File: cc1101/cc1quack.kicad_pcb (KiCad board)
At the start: 4 copper layers, 59 x 39 mm, 72 parts, among them J103 Conn_01x06_Pin, J201 USB_C_Receptacle, J401 Conn_ARM_JTAG_SWD_10, J402 Conn_01x02, J501 Conn_Coaxial, SW401 Alps SKRTLAE010, U301 XC6206P332MR, U401 STM32F401RCT6, U501 Ebyte-E07-900MM10S, Y401 8MHz 20pF

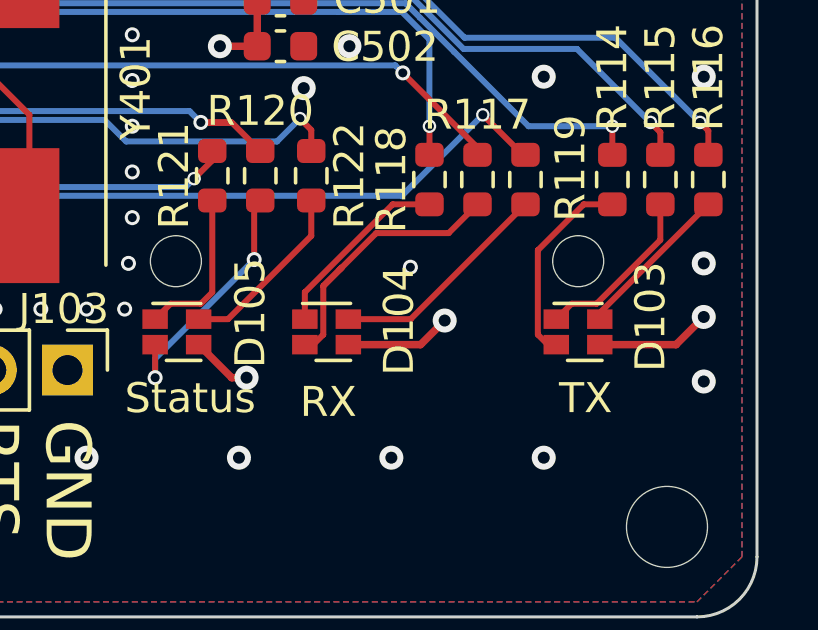
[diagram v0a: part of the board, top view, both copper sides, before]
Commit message: cc1quack: Specialize LiteOn LTST C19HE1WT footprint
Specialize LiteOn LTST C19HE1WT footprint to include 3D models.

Signed-off-by: Andreas Sandberg <andreas@sandberg.uk>
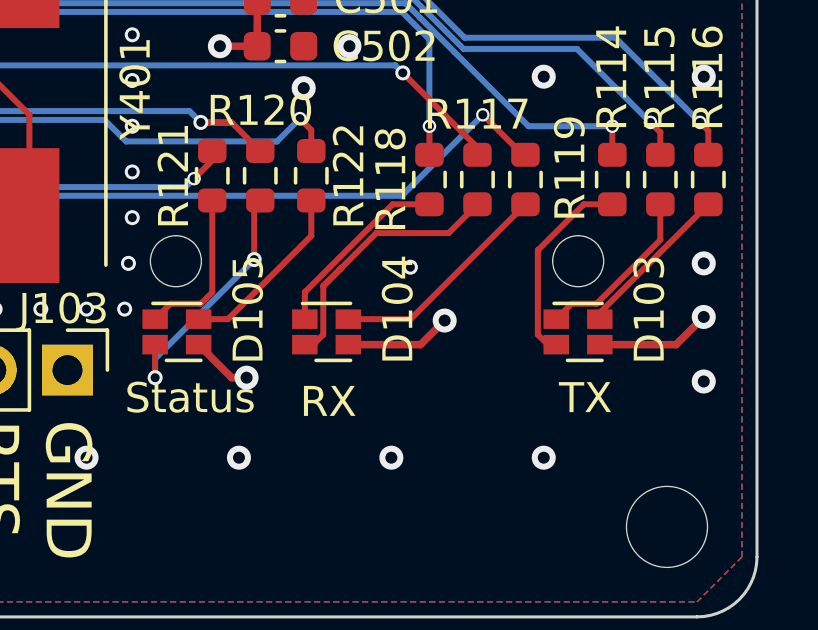
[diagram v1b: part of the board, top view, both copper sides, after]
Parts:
- D103, D104, D105: footprint LED_SMD:LED_LiteOn_LTST-C19HE1WT -> quack:LED_LiteOn_LTST-C19HE1WT
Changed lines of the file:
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@@
       (net 79 "/MCU/~{RF_CS}") (pinfunction "1") (pintype "passive"))
   )
-  (footprint "LED_SMD:LED_LiteOn_LTST-C19HE1WT" (layer "F.Cu")
+  (footprint "quack:LED_LiteOn_LTST-C19HE1WT" (layer "F.Cu")
     (at 139.663 79.5 90)
     (descr "LiteOn RGB LED; https://optoelectronics.liteon.com/upload/download/DS22-2008-0044/LTST-C19HE1WT.pdf")
@@
     (property "ki_keywords" "LED RGB diode")
     (attr smd)
-    (fp_text reference "D105" (at 0.633 2.45 90) (layer "F.SilkS")
+    (fp_text reference "D105" (at 0.748 2.3928 270) (layer "F.SilkS")
         (effects (font (size 1 1) (thickness 0.15)))
     )
@@
       (scale (xyz 1 1 1))
       (rotate (xyz 0 0 0))
+    )
+    (model "${KIPRJMOD}/3dmodels/LED_LiteOn_LTST-C19HE1WT.stp"
+      (offset (xyz 0 0 0))
+      (scale (xyz 1 1 1))
+      (rotate (xyz -90 0 90))
+    )
+    (model "${KIPRJMOD}/3dmodels/LED_LiteOn_LTST-C19HE1WT.wrl"
+      (offset (xyz 0 0 0))
+      (scale (xyz 1 1 1))
+      (rotate (xyz -90 0 90))
     )
   )
@@
     )
   )
-  (footprint "LED_SMD:LED_LiteOn_LTST-C19HE1WT" (layer "F.Cu")
+  (footprint "quack:LED_LiteOn_LTST-C19HE1WT" (layer "F.Cu")
     (at 153.035 79.5 90)
     (descr "LiteOn RGB LED; https://optoelectronics.liteon.com/upload/download/DS22-2008-0044/LTST-C19HE1WT.pdf")
@@
     (property "ki_keywords" "LED RGB diode")
     (attr smd)
-    (fp_text reference "D103" (at 0.506 2.413 90) (layer "F.SilkS")
+    (fp_text reference "D103" (at 0.748 2.3928 270) (layer "F.SilkS")
         (effects (font (size 1 1) (thickness 0.15)))
     )
@@
       (scale (xyz 1 1 1))
       (rotate (xyz 0 0 0))
+    )
+    (model "${KIPRJMOD}/3dmodels/LED_LiteOn_LTST-C19HE1WT.stp"
+      (offset (xyz 0 0 0))
+      (scale (xyz 1 1 1))
+      (rotate (xyz -90 0 90))
+    )
+    (model "${KIPRJMOD}/3dmodels/LED_LiteOn_LTST-C19HE1WT.wrl"
+      (offset (xyz 0 0 0))
+      (scale (xyz 1 1 1))
+      (rotate (xyz -90 0 90))
     )
   )
@@
     )
   )
-  (footprint "LED_SMD:LED_LiteOn_LTST-C19HE1WT" (layer "F.Cu")
+  (footprint "quack:LED_LiteOn_LTST-C19HE1WT" (layer "F.Cu")
     (at 144.653 79.5 90)
     (descr "LiteOn RGB LED; https://optoelectronics.liteon.com/upload/download/DS22-2008-0044/LTST-C19HE1WT.pdf")
@@
     (property "ki_keywords" "LED RGB diode")
     (attr smd)
-    (fp_text reference "D104" (at 0.379 2.413 270) (layer "F.SilkS")
+    (fp_text reference "D104" (at 0.748 2.3928 270) (layer "F.SilkS")
         (effects (font (size 1 1) (thickness 0.15)))
     )
@@
       (rotate (xyz 0 0 0))
     )
-  )
+    (model "${KIPRJMOD}/3dmodels/LED_LiteOn_LTST-C19HE1WT.stp"
+      (offset (xyz 0 0 0))
+      (scale (xyz 1 1 1))
+      (rotate (xyz -90 0 90))
+    )
+    (model "${KIPRJMOD}/3dmodels/LED_LiteOn_LTST-C19HE1WT.wrl"
+      (offset (xyz 0 0 0))
+      (scale (xyz 1 1 1))
+      (rotate (xyz -90 0 90))
+    )
+  )
